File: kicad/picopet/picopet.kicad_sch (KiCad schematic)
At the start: 32 parts, among them J1 Conn_01x14_Pin, J2 Conn_01x02_Socket, J3 Conn_01x02_Socket, J4 Conn_01x02_Socket, J5 USB_C_Receptacle_USB2.0_14P, M1 Motor_DC, SW1 SW_SPST, SW2 SW_Push, SW3 SW_Push, SW4 SW_Push, SW5 SW_Push, SW6 SW_Push, SW7 SW_Push, U1 RP2040, U2 W25Q32JVSS, U3 MCP73831-2-MC, U4 DS3231MZ, U5 BQ27427YZFR, U6 AT24CS32-SSHM, U8 XC6206PxxxMR, Y1 ASCO

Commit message: Updating schematics
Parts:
- removed BT1: RTC_Battery 3V, symbol Device:Battery_Cell
- removed BT2: Single Li-Ion Cell, symbol Device:Battery_Cell
- removed C2, C3: 1uF, symbol Device:C
- removed C4: 2.2uF, symbol Device:C
- removed J2, J3, J4: Conn_01x02_Socket, symbol Connector:Conn_01x02_Socket
- removed R10, R9: 5.1k, symbol Device:R
- removed R11, R12: 10k, symbol Device:R
- removed R8: 2K, symbol Device:R
- removed SW7: SW_Push, symbol Switch:SW_Push
- removed U1: RP2040, Package_DFN_QFN:QFN-56-1EP_7x7mm_P0.4mm_EP3.2x3.2mm, symbol MCU_RaspberryPi:RP2040
- removed U2: W25Q32JVSS, Package_SO:SOIC-8_5.3x5.3mm_P1.27mm, symbol Memory_Flash:W25Q32JVSS
- removed U3: MCP73831-2-MC, Package_DFN_QFN:DFN-8-1EP_3x2mm_P0.5mm_EP1.7x1.4mm, symbol Battery_Management:MCP73831-2-MC
- removed U5: BQ27427YZFR, DSBGA9-YZF_TEX, symbol 2025-03-19_04-45-52:BQ27427YZFR
- removed U8: XC6206PxxxMR, Package_TO_SOT_SMD:SOT-23-3, symbol Regulator_Linear:XC6206PxxxMR
- removed Y1: ASCO, Oscillator:Oscillator_SMD_Abracon_ASCO-4Pin_1.6x1.2mm, symbol Oscillator:ASCO
- added C1, C10, C12, C13, C16, C19, C5, C6, C7, C8: 100n, Capacitor_SMD:C_0402_1005Metric, symbol Device:C
- added C11, C9: 1u, Capacitor_SMD:C_0402_1005Metric, symbol Device:C
- added C14, C15: 4.7u, Capacitor_SMD:C_0805_2012Metric, symbol Device:C
- added C17, C18: 1u, Capacitor_SMD:C_0805_2012Metric, symbol Device:C
- added C20, C21: 27p, Capacitor_SMD:C_0402_1005Metric, symbol Device:C
- added J2: MicroJST 1.25mm female, Connector_JST:JST_GH_SM02B-GHS-TB_1x02-1MP_P1.25mm_Horizontal, symbol Connector_Generic:Conn_01x02
- added J3: CR1220 Holder, Battery:BatteryHolder_LINX_BAT-HLD-012-SMT, symbol Connector_Generic:Conn_01x02
- added R1, R13, R14, R15, R2, R5, R6, R7: 5.1k, symbol Device:R
- added R16, R18: 1k, Capacitor_SMD:C_0402_1005Metric, symbol Device:R
- added R17: DNF, Capacitor_SMD:C_0402_1005Metric, symbol Device:R
- added R3, R4: 27, Capacitor_SMD:C_0402_1005Metric, symbol Device:R
- added U1: RP2040, RP2040_minimal:RP2040-QFN-56, symbol MCU_RaspberryPi_RP2040:RP2040
- added U2: MCP73831-2-OT, Package_TO_SOT_SMD:SOT-23-5, symbol Battery_Management:MCP73831-2-OT
- added U3: S-T111B33MC-OGSTFU, Package_TO_SOT_SMD:SOT-23-5, symbol Regulator_Linear:TPS77012PDBV
- added U7: W25Q128JVS, Package_SO:SOIC-8_5.23x5.23mm_P1.27mm, symbol RP2040_minimal-rescue:W25Q128JVS-Memory_Flash
- added Y1: ABLS-12.000MHZ-B4-T, RP2040_minimal:Crystal_SMD_HC49-US, symbol Device:Crystal
- SW1: value SW_SPST -> PWR
- SW2: renamed from SW6; value SW_Push -> BOOTSEL
- SW4: renamed from SW2; value SW_Push -> Btn0
- SW5: renamed from SW3; value SW_Push -> Btn1
- SW6: renamed from SW4; value SW_Push -> Btn2
- SW7: renamed from SW5; value SW_Push -> Btn3
- renumbered J5 to J1, J1 to J4
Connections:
- net GND: now also J1.A1 (GND), J1.A12 (GND), J1.B1 (GND), J1.B12 (GND), J1.S1 (SHIELD), SW2.1, U4.5 (GND), U6.1 (A0), U6.2 (A1), U6.3 (A2), U6.4 (GND), U6.7 (WP), C1.2, C10.2, C11.2, C12.2, C13.2, C14.2, C15.2, C16.2, C17.2, C18.2, C19.2, C20.2, C21.2, C5.2, C6.2, C7.2, C8.2, C9.2, J2.2 (Pin_2), J3.2 (Pin_2), R1.2, R2.2, R5.1, U1.19 (TESTEN), U1.57 (GND), U2.2 (V_{SS}), U3.2 (GND), U3.4 (GND), U7.4 (GND)
- net VBAT: now also SW1.1 (A), C15.1, J2.1 (Pin_1), U2.3 (V_{BAT})
- net GPIO_0: now reaches U6.5 (SDA)
- net GPIO_0: now also U4.7 (SDA), R15.1, R7.1
- net GPIO_1: now reaches U6.6 (SCL)
- net GPIO_1: now also U4.8 (SCL), R14.1, R6.1
- net +3V3: now reaches U6.8 (VCC)
- net +3V3: now also U4.2 (VCC), C1.1, C10.1, C16.1, C17.1, C19.1, C5.1, C6.1, C7.1, C8.1, C9.1, R13.2, R14.2, R15.2, R17.1, R6.2, R7.2, U1.1 (IOVDD), U1.10 (IOVDD), U1.22 (IOVDD), U1.33 (IOVDD), U1.42 (IOVDD), U1.43 (ADC_AVDD), U1.44 (VREG_IN), U1.48 (USB_VDD), U1.49 (IOVDD), U3.5 (OUT), U7.8 (VCC)
- net GPIO_5: now reaches U4.3 (~{INT}/SQW)
- net GPIO_5: now also R13.1
- net VCOIN: now reaches U4.6 (VBAT)
- net VCOIN: now also J3.1 (Pin_1)
- net at SW2.2: now also R16.2
- net at J1.A4 (VBUS), J1.A9 (VBUS), J1.B4 (VBUS)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: now also C14.1, U2.4 (V_{DD})
- net at J1.A5 (CC1): now also R1.1
- net USB_D+: now reaches J1.A6 (D+)
- net USB_D+: now also J1.B6 (D+), R3.1
- net USB_D-: now reaches J1.A7 (D-)
- net USB_D-: now also J1.B7 (D-), R4.1
- net at J1.B5 (CC2): now also R2.1
- net at SW1.2 (B): now also C18.1, U3.1 (IN), U3.3 (EN)
- new net: R3.2, U1.47 (USB_DP)
- new net: R4.2, U1.46 (USB_DM)
- new net: C21.1, R18.2, Y1.2
- new net: R5.2, U2.5 (PROG)
- new net +1V1: C11.1, C12.1, C13.1, U1.23 (DVDD), U1.45 (VREG_VOUT), U1.50 (DVDD)
- new net GPIO0: U1.2 (GPIO0)
- new net GPIO1: U1.3 (GPIO1)
- new net GPIO10: U1.13 (GPIO10)
- new net GPIO11: U1.14 (GPIO11)
- new net GPIO12: U1.15 (GPIO12)
- new net GPIO13: U1.16 (GPIO13)
- new net GPIO14: U1.17 (GPIO14)
- new net GPIO15: U1.18 (GPIO15)
- new net GPIO16: U1.27 (GPIO16)
- new net GPIO17: U1.28 (GPIO17)
- new net GPIO18: U1.29 (GPIO18)
- new net GPIO19: U1.30 (GPIO19)
- new net GPIO2: U1.4 (GPIO2)
- new net GPIO20: U1.31 (GPIO20)
- new net GPIO21: U1.32 (GPIO21)
- new net GPIO22: U1.34 (GPIO22)
- new net GPIO23: U1.35 (GPIO23)
- new net GPIO24: U1.36 (GPIO24)
- new net GPIO25: U1.37 (GPIO25)
- new net GPIO26_ADC0: U1.38 (GPIO26_ADC0)
- new net GPIO27_ADC1: U1.39 (GPIO27_ADC1)
- new net GPIO28_ADC2: U1.40 (GPIO28_ADC2)
- new net GPIO29_ADC3: U1.41 (GPIO29_ADC3)
- new net GPIO3: U1.5 (GPIO3)
- new net GPIO4: U1.6 (GPIO4)
- new net GPIO5: U1.7 (GPIO5)
- new net GPIO6: U1.8 (GPIO6)
- new net GPIO7: U1.9 (GPIO7)
- new net GPIO8: U1.11 (GPIO8)
- new net GPIO9: U1.12 (GPIO9)
- new net GPIO_UNDECIDED: U2.1 (STAT)
- new net QSPI_SCLK: U1.52 (QSPI_SCLK), U7.6 (CLK)
- new net QSPI_SD0: U1.53 (QSPI_SD0), U7.5 (DI(IO0))
- new net QSPI_SD1: U1.55 (QSPI_SD1), U7.2 (DO(IO1))
- new net QSPI_SD2: U1.54 (QSPI_SD2), U7.3 (IO2)
- new net QSPI_SD3: U1.51 (QSPI_SD3), U7.7 (IO3)
- new net QSPI_SS: R16.1, R17.2, U1.56 (QSPI_SS), U7.1 (~{CS})
- new net RUN: U1.26 (RUN)
- new net SWCLK: U1.24 (SWCLK)
- new net SWD: U1.25 (SWD)
- new net XIN: C20.1, U1.20 (XIN), Y1.1
- new net XOUT: R18.1, U1.21 (XOUT)
- no-connect marks 0 -> 2
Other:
- note added: "Make sure C11 is close to pin 45 of RP2040"
- note added: "Make sure C9 is close to pin 44 of RP2040"
- note added: "Make sure R3 and R4 are close to RP2040"
- moved on the sheet: BZ1, J1, J4, M1, SW1, SW2, SW4, SW5, SW6, SW7, U4

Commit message: More schematic work
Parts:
- removed J4: Conn_01x14_Pin, symbol Connector:Conn_01x14_Pin
- added C2: 1u, Capacitor_SMD:C_0805_2012Metric, symbol Device:C
- added J4: ST7735 LCD, custom:ST7735_P0.8mm, symbol custom:ST7735
- added Q1: SS8050, Package_TO_SOT_SMD:SOT-23, symbol Transistor_BJT:SS8050
- added R10: 10, symbol Device:R
- added R11: 10K, symbol Device:R
- added R12: 1K, symbol Device:R
- added R8, R9: 100k, symbol Device:R
- BZ1: footprint (none) -> Buzzer_Beeper:MagneticBuzzer_CUI_CMT-8504-100-SMT
- J1: footprint (none) -> Connector_USB:USB_C_Receptacle_G-Switch_GT-USB-7025
- M1: footprint (none) -> Connector_JST:JST_GH_SM02B-GHS-TB_1x02-1MP_P1.25mm_Horizontal
- SW1: footprint (none) -> Button_Switch_THT:SW_Slide_SPDT_Angled_CK_OS102011MA1Q
- SW4, SW5, SW6, SW7: footprint (none) -> Button_Switch_SMD:SW_SPST_EVQP2_MiddlePushTravel_H2.5mm
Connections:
- net +3V3: now also C2.1, J4.10 (VCC), J4.11 (IOVCC), J4.4 (LED+), R11.1
- net GND: now also BZ1.2 (-), M1.2 (-), SW4.2, SW5.2, SW6.2, SW7.2, C2.2, J4.13 (GND), J4.2 (GND), J4.5 (GND), Q1.2 (E), R9.1
- net GPIO_UNDECIDED: now also R8.1, R9.2
- net GPIO_6: now reaches M1.1 (+)
- net GPIO_15: now reaches SW4.1
- net GPIO_4: now reaches BZ1.1 (+)
- net GPIO_2: now reaches SW6.1
- net VSENSE: now reaches C18.1, SW1.2 (B), U3.1 (IN), U3.3 (EN)
- net VSENSE: now also R8.2
- net GPIO_3: now reaches SW7.1
- net GPIO_17: now reaches SW5.1
- new net: Q1.1 (B), R11.2, R12.1
- new net: J4.3 (LED-), R10.1
- new net: Q1.3 (C), R10.2
- new net GPIO_10: J4.9 (CLK)
- new net GPIO_11: J4.8 (DIN)
- new net GPIO_12: J4.6 (~RESET)
- new net GPIO_13: R12.2
- new net GPIO_8: J4.7 (A0)
- new net GPIO_9: J4.12 (CS)
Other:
- moved on the sheet: BZ1, M1, SW1, SW4, SW5, SW6, SW7

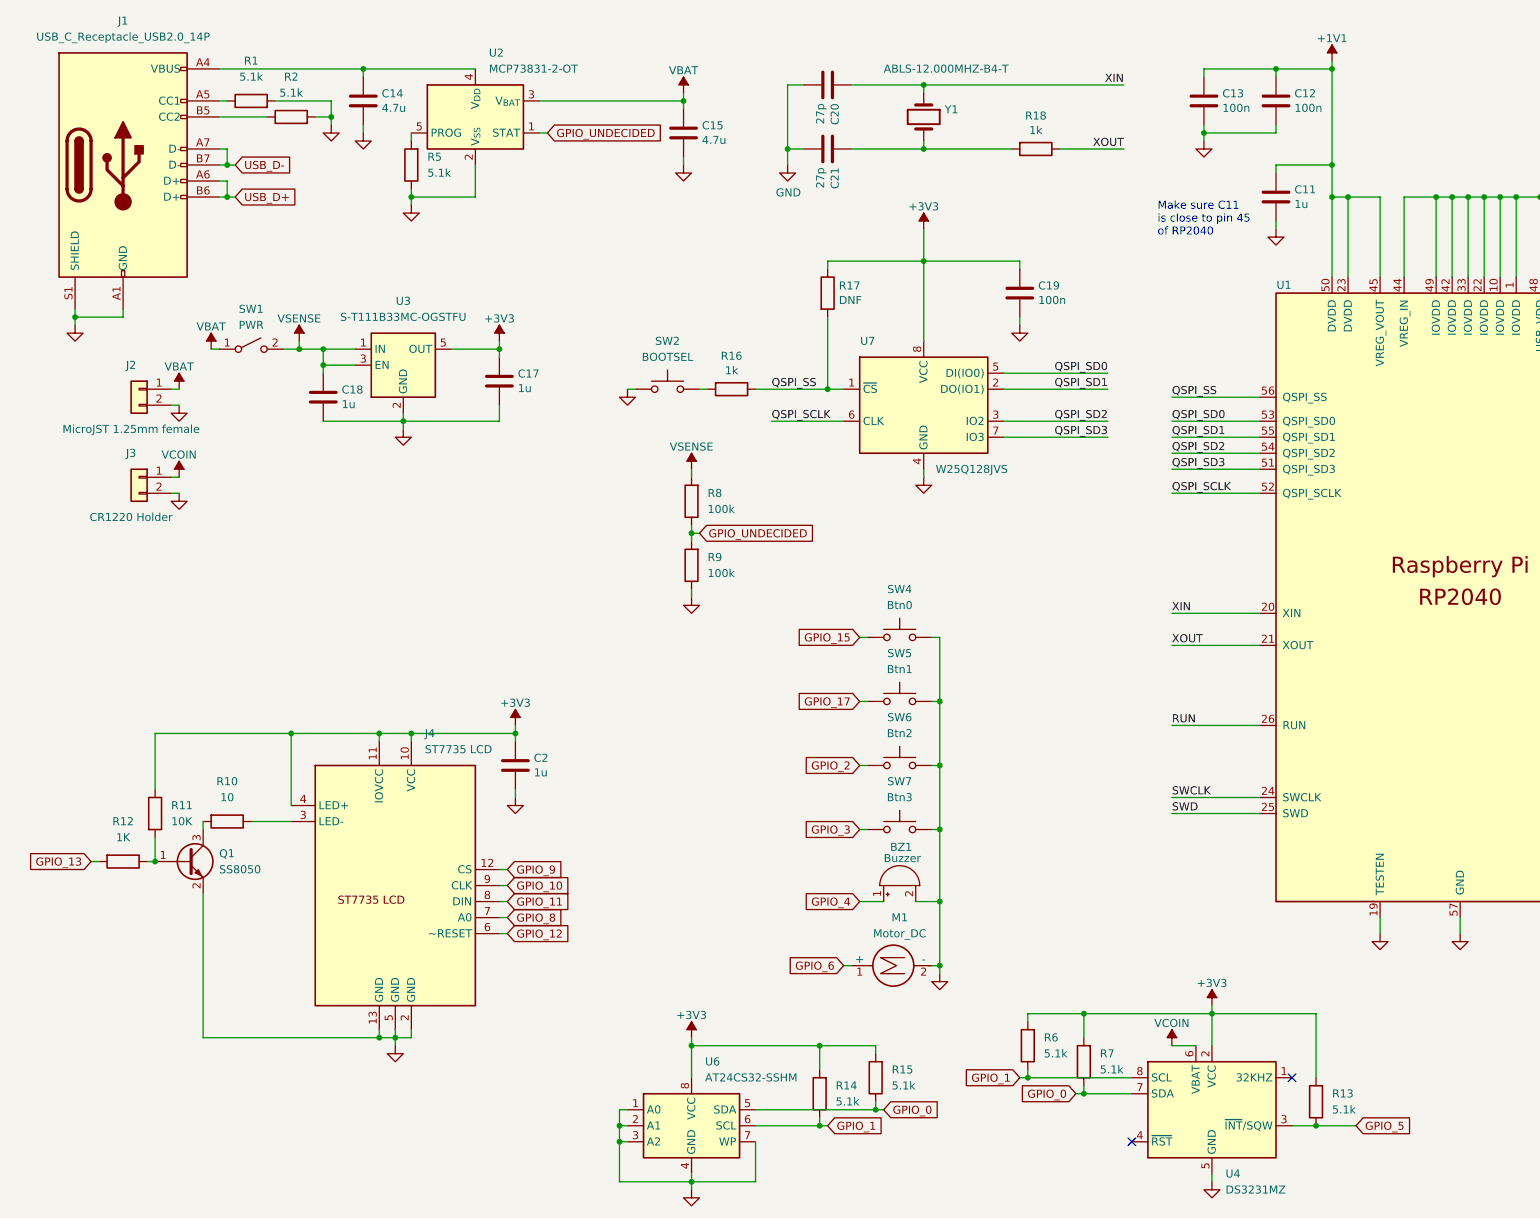
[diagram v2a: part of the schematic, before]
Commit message: Working on a PCB layout, but didn't plan the LCD well enough
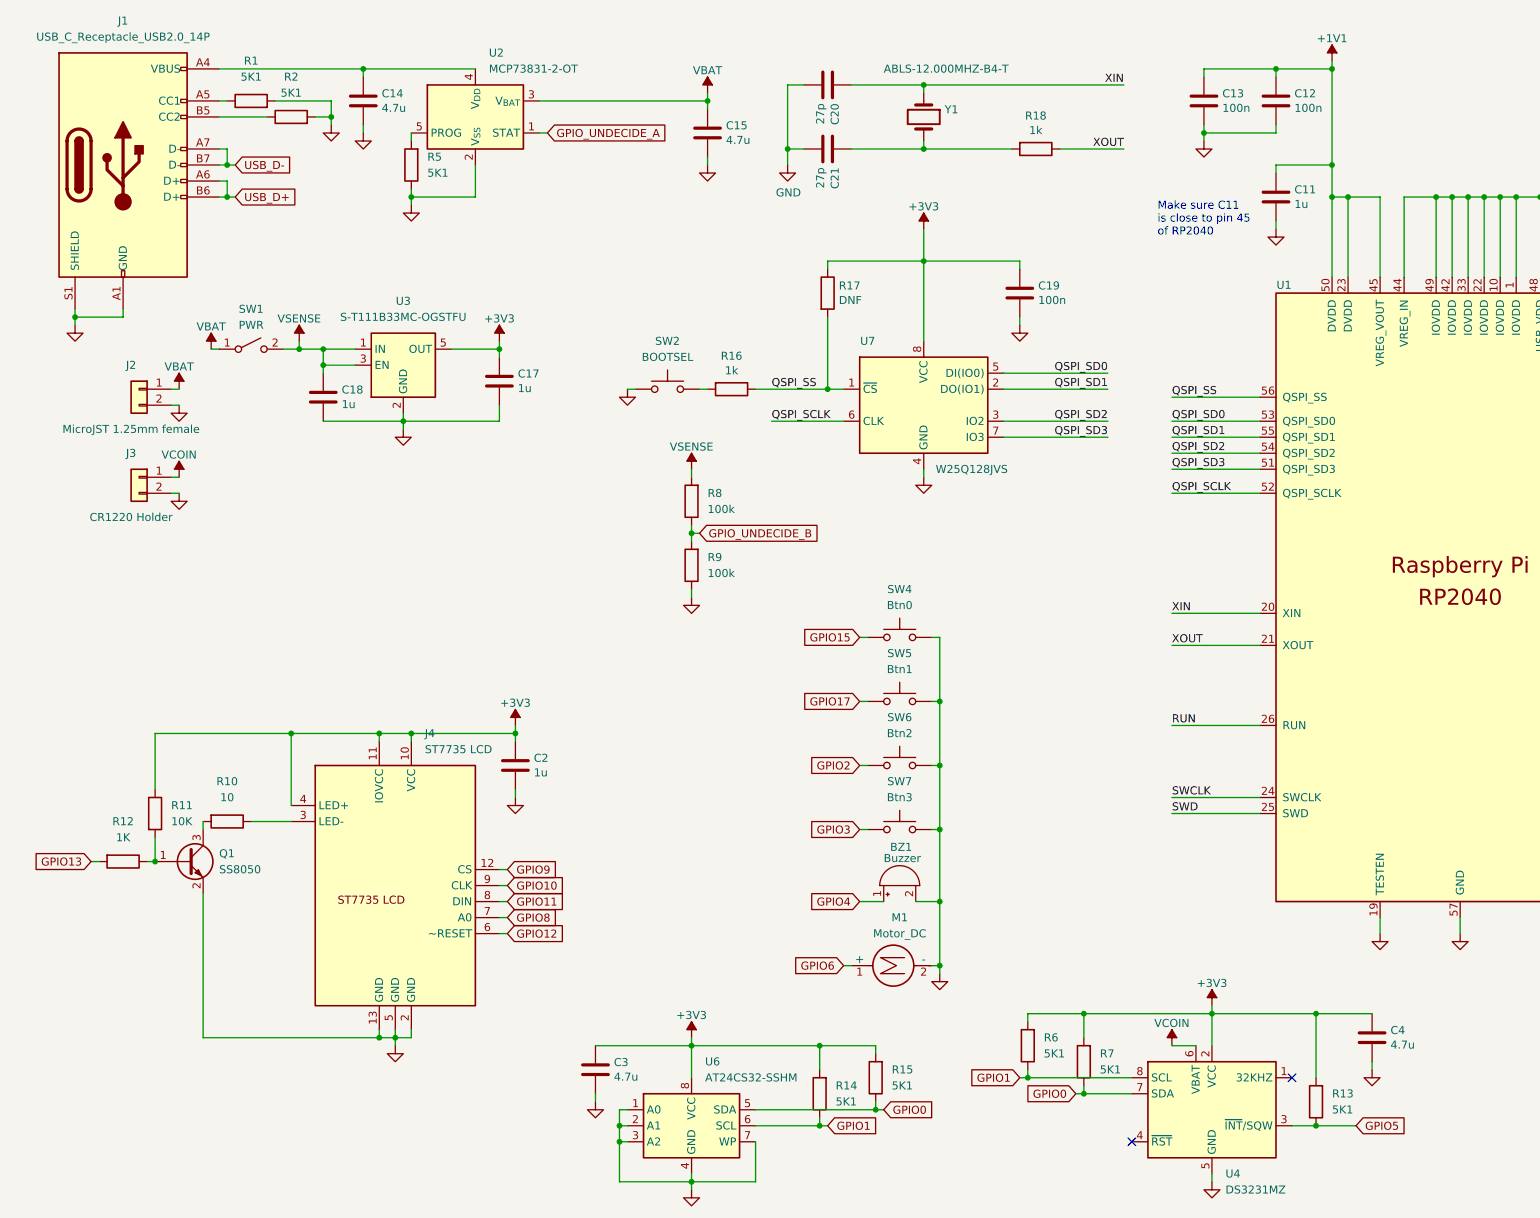
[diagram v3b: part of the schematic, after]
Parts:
- added C3, C4: 4.7u, Capacitor_SMD:C_0805_2012Metric, symbol Device:C
- J1: footprint Connector_USB:USB_C_Receptacle_G-Switch_GT-USB-7025 -> Connector_USB:USB_C_Receptacle_GCT_USB4105-xx-A_16P_TopMnt_Horizontal
- R1, R13, R14, R15, R2, R5, R6, R7: value 5.1k -> 5K1; footprint (none) -> Resistor_SMD:R_0402_1005Metric
- R10, R11, R12, R8, R9: footprint (none) -> Resistor_SMD:R_0402_1005Metric
- R16, R17, R18: footprint Capacitor_SMD:C_0402_1005Metric -> Resistor_SMD:R_0402_1005Metric
- R3, R4: footprint Capacitor_SMD:C_0402_1005Metric -> Resistor_SMD:R_0201_0603Metric
- SW2: footprint (none) -> Button_Switch_SMD:SW_SPST_EVQP2_MiddlePushTravel_H2.5mm
- U1: footprint RP2040_minimal:RP2040-QFN-56 -> Package_DFN_QFN:QFN-56-1EP_7x7mm_P0.4mm_EP3.2x3.2mm
- U7: footprint Package_SO:SOIC-8_5.23x5.23mm_P1.27mm -> Package_SO:SOIC-8_5.3x5.3mm_P1.27mm
- Y1: footprint RP2040_minimal:Crystal_SMD_HC49-US -> Crystal:Crystal_SMD_HC49-SD
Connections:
- net GPIO_0 is gone; now on net GPIO0: R15.1, R7.1, U4.7 (SDA), U6.5 (SDA)
- net GPIO_1 is gone; now on net GPIO1: R14.1, R6.1, U4.8 (SCL), U6.6 (SCL)
- net GPIO_10 is gone; now on net GPIO10: J4.9 (CLK)
- net GPIO_11 is gone; now on net GPIO11: J4.8 (DIN)
- net GPIO_12 is gone; now on net GPIO12: J4.6 (~RESET)
- net GPIO_13 is gone; now on net GPIO13: R12.2
- net GPIO_15 is gone; now on net GPIO15: SW4.1
- net GPIO_17 is gone; now on net GPIO17: SW5.1
- net GPIO_2 is gone; now on net GPIO2: SW6.1
- net GPIO_3 is gone; now on net GPIO3: SW7.1
- net GPIO_4 is gone; now on net GPIO4: BZ1.1 (+)
- net GPIO_5 is gone; now on net GPIO5: R13.1, U4.3 (~{INT}/SQW)
- net GPIO_6 is gone; now on net GPIO6: M1.1 (+)
- net GPIO_8 is gone; now on net GPIO8: J4.7 (A0)
- net GPIO_9 is gone; now on net GPIO9: J4.12 (CS)
- net +3V3: now also C3.1, C4.1
- net GND: now also C3.2, C4.2
- net GPIO_UNDECIDED renamed GPIO_UNDECIDE_B
- net GPIO_UNDECIDE_B: no longer U2.1 (STAT)
- new net GPIO_UNDECIDE_A: U2.1 (STAT)
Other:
- moved on the sheet: C15

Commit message: Redesigning pcb
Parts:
- removed C2: 1u, Capacitor_SMD:C_0805_2012Metric, symbol Device:C
- removed C3, C4: 4.7u, Capacitor_SMD:C_0805_2012Metric, symbol Device:C
- removed J4: ST7735 LCD, custom:ST7735_P0.8mm, symbol custom:ST7735
- removed M1: Motor_DC, Connector_JST:JST_GH_SM02B-GHS-TB_1x02-1MP_P1.25mm_Horizontal, symbol Motor:Motor_DC
- removed R1, R2: 5K1, Resistor_SMD:R_0402_1005Metric, symbol Device:R
- removed R12: 1K, Resistor_SMD:R_0402_1005Metric, symbol Device:R
- removed R17: DNF, Resistor_SMD:R_0402_1005Metric, symbol Device:R
- removed SW1: PWR, Button_Switch_THT:SW_Slide_SPDT_Angled_CK_OS102011MA1Q, symbol Switch:SW_SPST
- added C15: 2u2, Capacitor_SMD:C_0402_1005Metric, symbol Device:C
- added C16: 1u, Capacitor_SMD:C_0402_1005Metric, symbol Device:C
- added C21: 4.7u, Capacitor_SMD:C_0805_2012Metric, symbol Device:C
- added J4: CR1220 Holder, Battery:BatteryHolder_LINX_BAT-HLD-012-SMT, symbol Connector_Generic:Conn_01x02
- added J5: ST7735 LCD, custom:ST7735_P0.8mm, symbol custom:ST7735
- added R5: 10, Resistor_SMD:R_0201_0603Metric, symbol Device:R
- added SW1: PWR, Button_Switch_SMD:SW_SPDT_CK_JS102011SAQN, symbol Switch:SW_SPDT
- C12: renamed from C20; value 27p -> 15p
- C13: renamed from C21; value 27p -> 15p
- J2: value MicroJST 1.25mm female -> PH1.25mm 2P
- J3: value CR1220 Holder -> PH1.25mm 2P; footprint Battery:BatteryHolder_LINX_BAT-HLD-012-SMT -> Connector_JST:JST_GH_SM02B-GHS-TB_1x02-1MP_P1.25mm_Horizontal
- R10: value 10 -> 5k1; footprint Resistor_SMD:R_0402_1005Metric -> Resistor_SMD:R_0201_0603Metric
- R11: value 10K -> 5k1; footprint Resistor_SMD:R_0402_1005Metric -> Resistor_SMD:R_0201_0603Metric
- R12: renamed from R5; value 5K1 -> 5k1; footprint Resistor_SMD:R_0402_1005Metric -> Resistor_SMD:R_0201_0603Metric
- R13, R14, R15: footprint Resistor_SMD:R_0402_1005Metric -> Resistor_SMD:R_0201_0603Metric
- R4: renamed from R16; footprint Resistor_SMD:R_0402_1005Metric -> Resistor_SMD:R_0201_0603Metric
- R6: value 5K1 -> 10k; footprint Resistor_SMD:R_0402_1005Metric -> Resistor_SMD:R_0201_0603Metric
- R7: value 5K1 -> 1k; footprint Resistor_SMD:R_0402_1005Metric -> Resistor_SMD:R_0201_0603Metric
- U7: value W25Q128JVS -> W25Q32JVSSIQ; footprint Package_SO:SOIC-8_5.3x5.3mm_P1.27mm -> Package_SO:SOIC-8-1EP_3.9x4.9mm_P1.27mm_EP2.29x3mm
- Y1: value ABLS-12.000MHZ-B4-T -> X322512MSB4SI; footprint Crystal:Crystal_SMD_HC49-SD -> Crystal:Crystal_SMD_3225-4Pin_3.2x2.5mm
- renumbered C12 to C10, C13 to C11, C19 to C14, C15 to C19, C5 to C2, C14 to C20, C6 to C3, C16 to C4, C7 to C5, C8 to C6, C10 to C7, C9 to C8, C11 to C9, R3 to R1, R4 to R2, R18 to R3, SW4 to SW3, SW5 to SW4, SW6 to SW5, SW7 to SW6
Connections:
- net GPIO_UNDECIDE_A is gone; now on net GPIO25: U2.1 (STAT)
- net +3V3: now also C15.2, C16.2, C21.1, J5.10 (VCC), J5.11 (IOVCC), J5.4 (LED+); no longer R11.1, R7.2
- net GND: now also J3.1 (Pin_1), R10.2, R11.2, SW2.2, C15.1, C16.1, C21.2, J4.2 (Pin_2), J5.13 (GND), J5.2 (GND), J5.5 (GND); no longer J3.2 (Pin_2), SW2.1
- net GPIO0: no longer R7.1
- net GPIO1: no longer R6.1
- net GPIO10: now also J5.9 (CLK)
- net GPIO11: now also J5.8 (DIN)
- net GPIO12: now also J5.6 (~{RESET})
- net GPIO13: now also R7.1
- net GPIO6: now also J3.2 (Pin_2)
- net GPIO8: now also J5.7 (A0)
- net GPIO9: now also J5.12 (CS)
- net VBAT: now also SW1.2 (B)
- net VCOIN: now also J4.1 (Pin_1); no longer J3.1 (Pin_1)
- net VSENSE: now also SW1.1 (A)
- net USBC_VDD: now reaches C20.1, J1.A4 (VBUS), J1.A9 (VBUS), J1.B4 (VBUS), J1.B9 (VBUS), U2.4 (V_{DD})
- net at Q1.1 (B): now also R6.1, R7.2; no longer R11.2
- net at R4.2: now also SW2.1; no longer SW2.2
- net at R10.1: now also J1.A5 (CC1)
- net at J1.B5 (CC2): now also R11.1
- net at Q1.3 (C): now also R5.1; no longer R10.2
- net GPIO_UNDECIDE_B renamed GPIO26
- new net: J5.3 (LED-), R5.2
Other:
- note added: "Make sure C8 is close to pin 44 of RP2040"
- note added: "Make sure C9 is close to pin 45 of RP2040"
- note added: "Make sure R1 and R2 are close to RP2040"
- note removed: "Make sure C11 is close to pin 45 of RP2040"
- note removed: "Make sure C9 is close to pin 44 of RP2040"
- note removed: "Make sure R3 and R4 are close to RP2040"
- moved on the sheet: BZ1, C1, C10, C11, C12, C13, C14, C17, C18, C19, C2, C20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

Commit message: Redesigning pcb
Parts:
- U7: footprint Package_SO:SOIC-8-1EP_3.9x4.9mm_P1.27mm_EP2.29x3mm -> Package_SO:SOIC-8_3.9x4.9mm_P1.27mm
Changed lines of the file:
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@@
 			)
 		)
-		(property "Footprint" "Package_SO:SOIC-8-1EP_3.9x4.9mm_P1.27mm_EP2.29x3mm"
+		(property "Footprint" "Package_SO:SOIC-8_3.9x4.9mm_P1.27mm"
 			(at 85.09 187.96 0)
 			(effects

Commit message: Various kicad edits
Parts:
- BZ1: footprint Buzzer_Beeper:MagneticBuzzer_CUI_CMT-8504-100-SMT -> Buzzer_Beeper:MagneticBuzzer_Kobitone_254-EMB84Q-RO
- SW1: footprint Button_Switch_SMD:SW_SPDT_CK_JS102011SAQN -> Button_Switch_THT:SW_Slide_SPDT_Angled_CK_OS102011MA1Q
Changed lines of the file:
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@@
 			)
 		)
-		(property "Footprint" "Button_Switch_SMD:SW_SPDT_CK_JS102011SAQN"
+		(property "Footprint" "Button_Switch_THT:SW_Slide_SPDT_Angled_CK_OS102011MA1Q"
 			(at 187.96 189.23 0)
 			(effects
@@
 			)
 		)
-		(property "Footprint" "Buzzer_Beeper:MagneticBuzzer_CUI_CMT-8504-100-SMT"
+		(property "Footprint" "Buzzer_Beeper:MagneticBuzzer_Kobitone_254-EMB84Q-RO"
 			(at 193.04 62.865 90)
 			(effects
